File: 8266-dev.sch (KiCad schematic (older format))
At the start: 17 parts, among them J1 USB_B_Micro, U1 ESP8266-12F_ESP-12F, U2 FT231XS

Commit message: updated to v1
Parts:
- removed C3: 0.1uF, symbol Device:C
- removed C4: 10uF, symbol Device:C
- removed C5, C6: C, symbol Device:C
- removed J1: USB_B_Micro, symbol Connector:USB_B_Micro
- removed R5, R6: R, symbol Device:R
- removed U2: FT231XS, Package_SO:SSOP-20_3.9x8.7mm_P0.635mm, symbol Interface_USB:FT231XS
- added J1, J2: Conn_01x05_Female, digikey-kicad-library:PinHeader_1x5_P2.5mm_Drill1.1mm, symbol Connector:Conn_01x05_Female
- added J3: Conn_01x06_Female, Connector_PinHeader_2.54mm:PinHeader_1x06_P2.54mm_Vertical, symbol Connector:Conn_01x06_Female
- added J4: Conn_01x03_Female, digikey-kicad-library:PinHeader_1x3_P2.54_Drill1.1mm, symbol Connector:Conn_01x03_Female
- BT1: footprint (none) -> Battery:BatteryHolder_MPD_BC2003_1x2032
- C2: footprint Capacitor_SMD:C_0603_1608Metric -> Capacitor_SMD:C_1206_3216Metric
- S1: footprint 430152070826:430152070826 -> digikey-kicad-library:Switch_Tactile_SMD_6x6mm
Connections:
- net labels added: ADC, CS0, IO10, IO12, IO13, IO14, IO16, IO2, IO4, IO5, IO9, MISO, MOSI, SCLK, rx, tx
- net labels removed: +3V3, D+, D-, RXD, TXD
- wire segments 41 -> 15
- no-connect marks 16 -> 2
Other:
- note removed: "FT231X IC"
- note removed: "USB INPUT"
- moved on the sheet: R3, S1

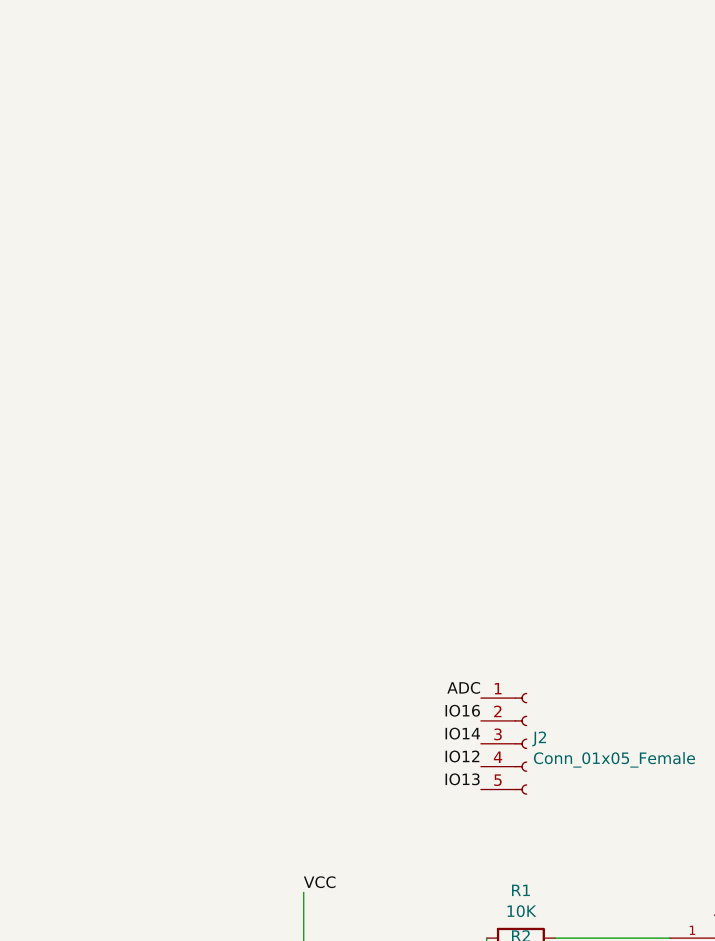
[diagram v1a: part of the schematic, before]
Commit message: added logic level shifter and some WS2812B's
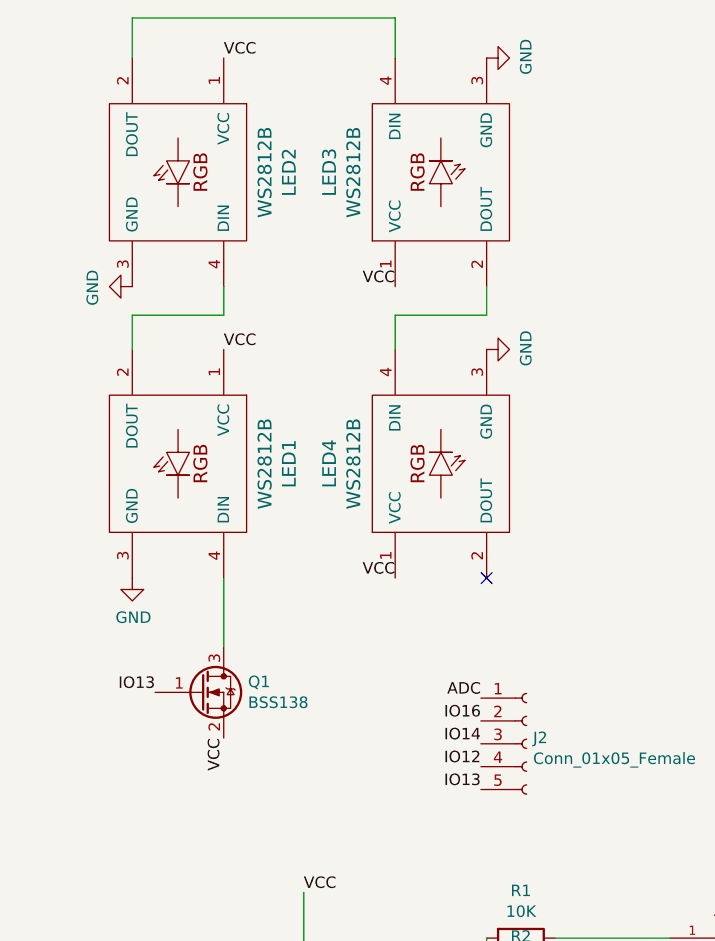
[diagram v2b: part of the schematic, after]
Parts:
- added LED1, LED2, LED3, LED4: WS2812B, LED_SMD:LED_WS2812B_PLCC4_5.0x5.0mm_P3.2mm, symbol ws2812b:WS2812B
- added Q1: BSS138, Package_TO_SOT_SMD:SOT-23, symbol Transistor_FET:BSS138
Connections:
- wire segments 15 -> 25
- no-connect marks 2 -> 3
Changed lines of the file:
@@
 Text Label 4800 6250 1    50   ~ 0
 SCLK
+Text Label 1900 3725 3    50   ~ 0
+VCC
+$Comp
+L Transistor_FET:BSS138 Q1
+U 1 1 5D2FF3C8
+P 1800 3525
+F 0 "Q1" H 2006 3571 50  0000 L CNN
+F 1 "BSS138" H 2006 3480 50  0000 L CNN
+F 2 "Package_TO_SOT_SMD:SOT-23" H 2000 3450 50  0001 L CIN
+F 3 "https://www.fairchildsemi.com/datasheets/BS/BSS138.pdf" H 1800 3525 50  0001 L CNN
+	1    1800 3525
+	1    0    0    -1
+$EndComp
+$Comp
+L ws2812b:WS2812B LED1
+U 1 1 5D31BE71
+P 1700 2525
+F 0 "LED1" H 1700 3012 60  0000 C CNN
+F 1 "WS2812B" H 1700 2906 60  0000 C CNN
+F 2 "LED_SMD:LED_WS2812B_PLCC4_5.0x5.0mm_P3.2mm" V 1650 2525 60  0001 C CNN
+F 3 "" V 1650 2525 60  0000 C CNN
+	1    1700 2525
+	0    1    1    0
+$EndComp
+Wire Wire Line
+	1900 3325 1900 3025
+$Comp
+L power:GND #PWR01
+U 1 1 5D31F7E8
+P 1500 3025
+F 0 "#PWR01" H 1500 2775 50  0001 C CNN
+F 1 "GND" H 1505 2852 50  0000 C CNN
+F 2 "" H 1500 3025 50  0001 C CNN
+F 3 "" H 1500 3025 50  0001 C CNN
+	1    1500 3025
+	1    0    0    -1
+$EndComp
+Text Label 1600 3525 2    50   ~ 0
+IO13
+Text Label 1900 2025 0    50   ~ 0
+VCC
+Text Label 1900 750  0    50   ~ 0
+VCC
+$Comp
+L ws2812b:WS2812B LED2
+U 1 1 5D33F0B1
+P 1700 1250
+F 0 "LED2" H 1700 1737 60  0000 C CNN
+F 1 "WS2812B" H 1700 1631 60  0000 C CNN
+F 2 "LED_SMD:LED_WS2812B_PLCC4_5.0x5.0mm_P3.2mm" V 1650 1250 60  0001 C CNN
+F 3 "" V 1650 1250 60  0000 C CNN
+	1    1700 1250
+	0    1    1    0
+$EndComp
+Wire Wire Line
+	1500 2025 1500 1875
+Wire Wire Line
+	1500 1875 1900 1875
+Wire Wire Line
+	1900 1875 1900 1750
+$Comp
+L power:GND #PWR02
+U 1 1 5D343D9C
+P 1500 1750
+F 0 "#PWR02" H 1500 1500 50  0001 C CNN
+F 1 "GND" H 1505 1577 50  0000 C CNN
+F 2 "" H 1500 1750 50  0001 C CNN
+F 3 "" H 1500 1750 50  0001 C CNN
+	1    1500 1750
+	0    1    1    0
+$EndComp
+$Comp
+L ws2812b:WS2812B LED3
+U 1 1 5D3463F4
+P 2850 1250
+F 0 "LED3" H 2850 1737 60  0000 C CNN
+F 1 "WS2812B" H 2850 1631 60  0000 C CNN
+F 2 "LED_SMD:LED_WS2812B_PLCC4_5.0x5.0mm_P3.2mm" V 2800 1250 60  0001 C CNN
+F 3 "" V 2800 1250 60  0000 C CNN
+	1    2850 1250
+	0    -1   -1   0
+$EndComp
+Text Label 2650 1750 2    50   ~ 0
+VCC
+$Comp
+L power:GND #PWR03
+U 1 1 5D347748
+P 3050 750
+F 0 "#PWR03" H 3050 500 50  0001 C CNN
+F 1 "GND" H 3055 577 50  0000 C CNN
+F 2 "" H 3050 750 50  0001 C CNN
+F 3 "" H 3050 750 50  0001 C CNN
+	1    3050 750
+	0    -1   -1   0
+$EndComp
+Wire Wire Line
+	1500 750  1500 575
+Wire Wire Line
+	1500 575  2650 575
+Wire Wire Line
+	2650 575  2650 750
+$Comp
+L ws2812b:WS2812B LED4
+U 1 1 5D34B87E
+P 2850 2525
+F 0 "LED4" H 2850 3012 60  0000 C CNN
+F 1 "WS2812B" H 2850 2906 60  0000 C CNN
+F 2 "LED_SMD:LED_WS2812B_PLCC4_5.0x5.0mm_P3.2mm" V 2800 2525 60  0001 C CNN
+F 3 "" V 2800 2525 60  0000 C CNN
+	1    2850 2525
+	0    -1   -1   0
+$EndComp
+$Comp
+L power:GND #PWR04
+U 1 1 5D34DD79
+P 3050 2025
+F 0 "#PWR04" H 3050 1775 50  0001 C CNN
+F 1 "GND" H 3055 1852 50  0000 C CNN
+F 2 "" H 3050 2025 50  0001 C CNN
+F 3 "" H 3050 2025 50  0001 C CNN
+	1    3050 2025
+	0    -1   -1   0
+$EndComp
+Text Label 2650 3025 2    50   ~ 0
+VCC
+Wire Wire Line
+	3050 1750 3050 1875
+Wire Wire Line
+	3050 1875 2650 1875
+Wire Wire Line
+	2650 1875 2650 2025
+NoConn ~ 3050 3025
 $EndSCHEMATC

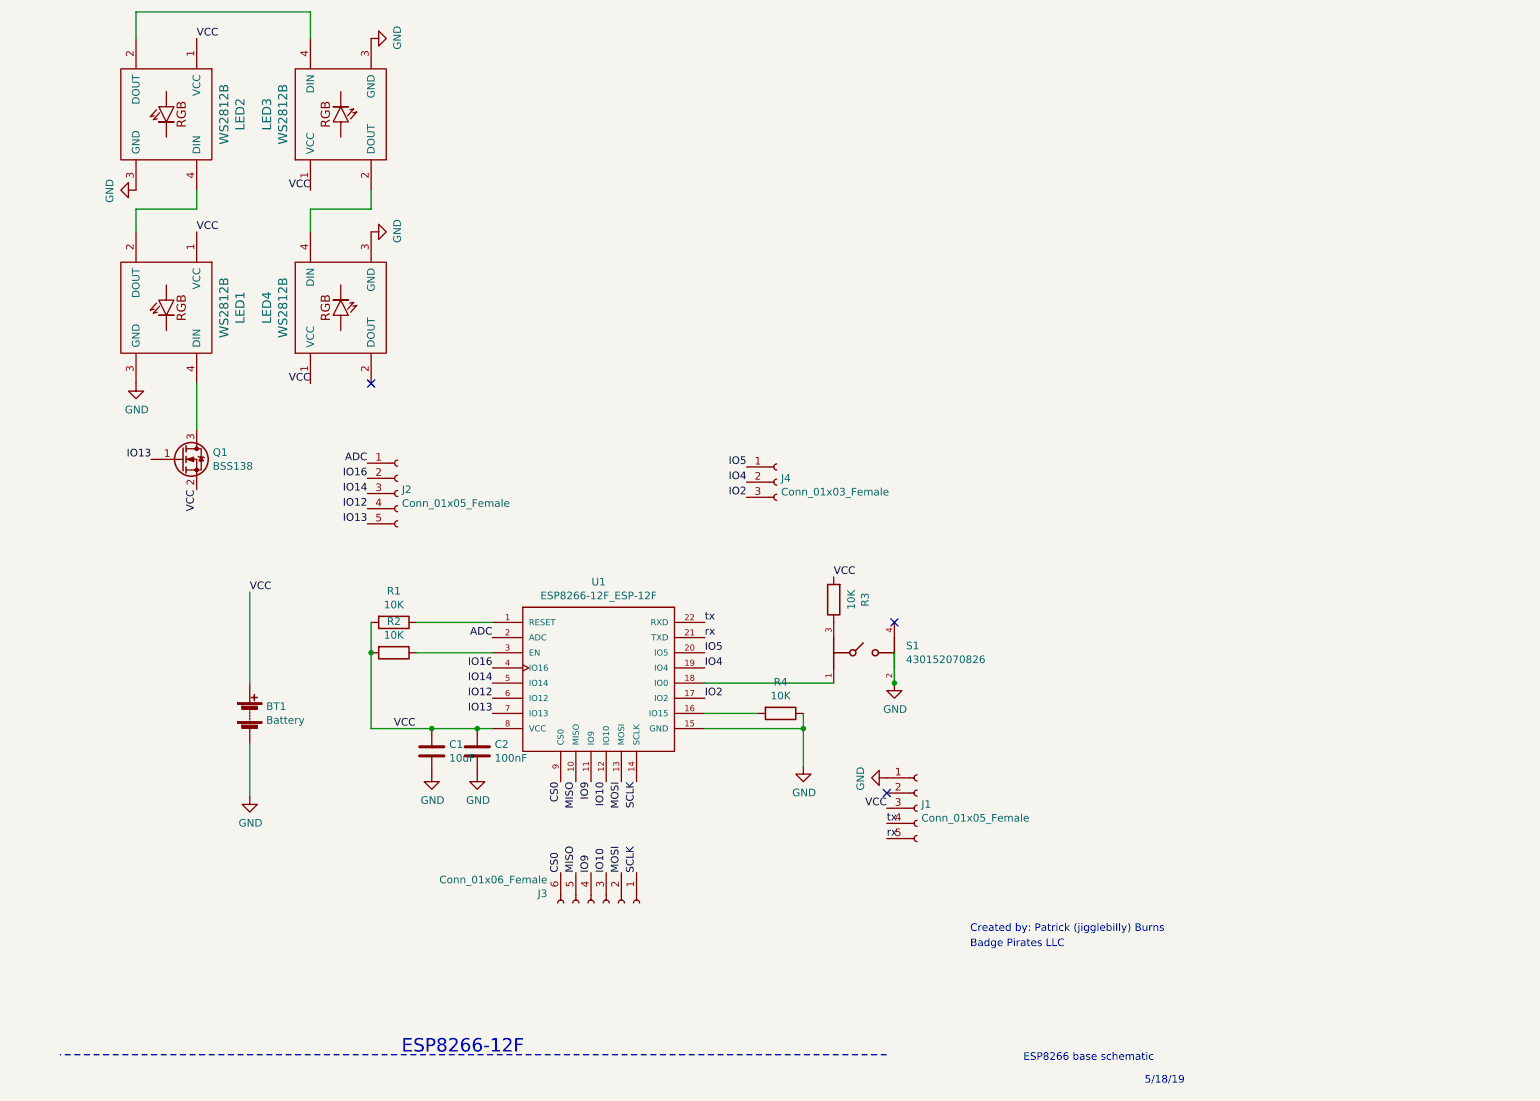
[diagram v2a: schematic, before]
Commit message: added power light, CH330N, and some neopixels
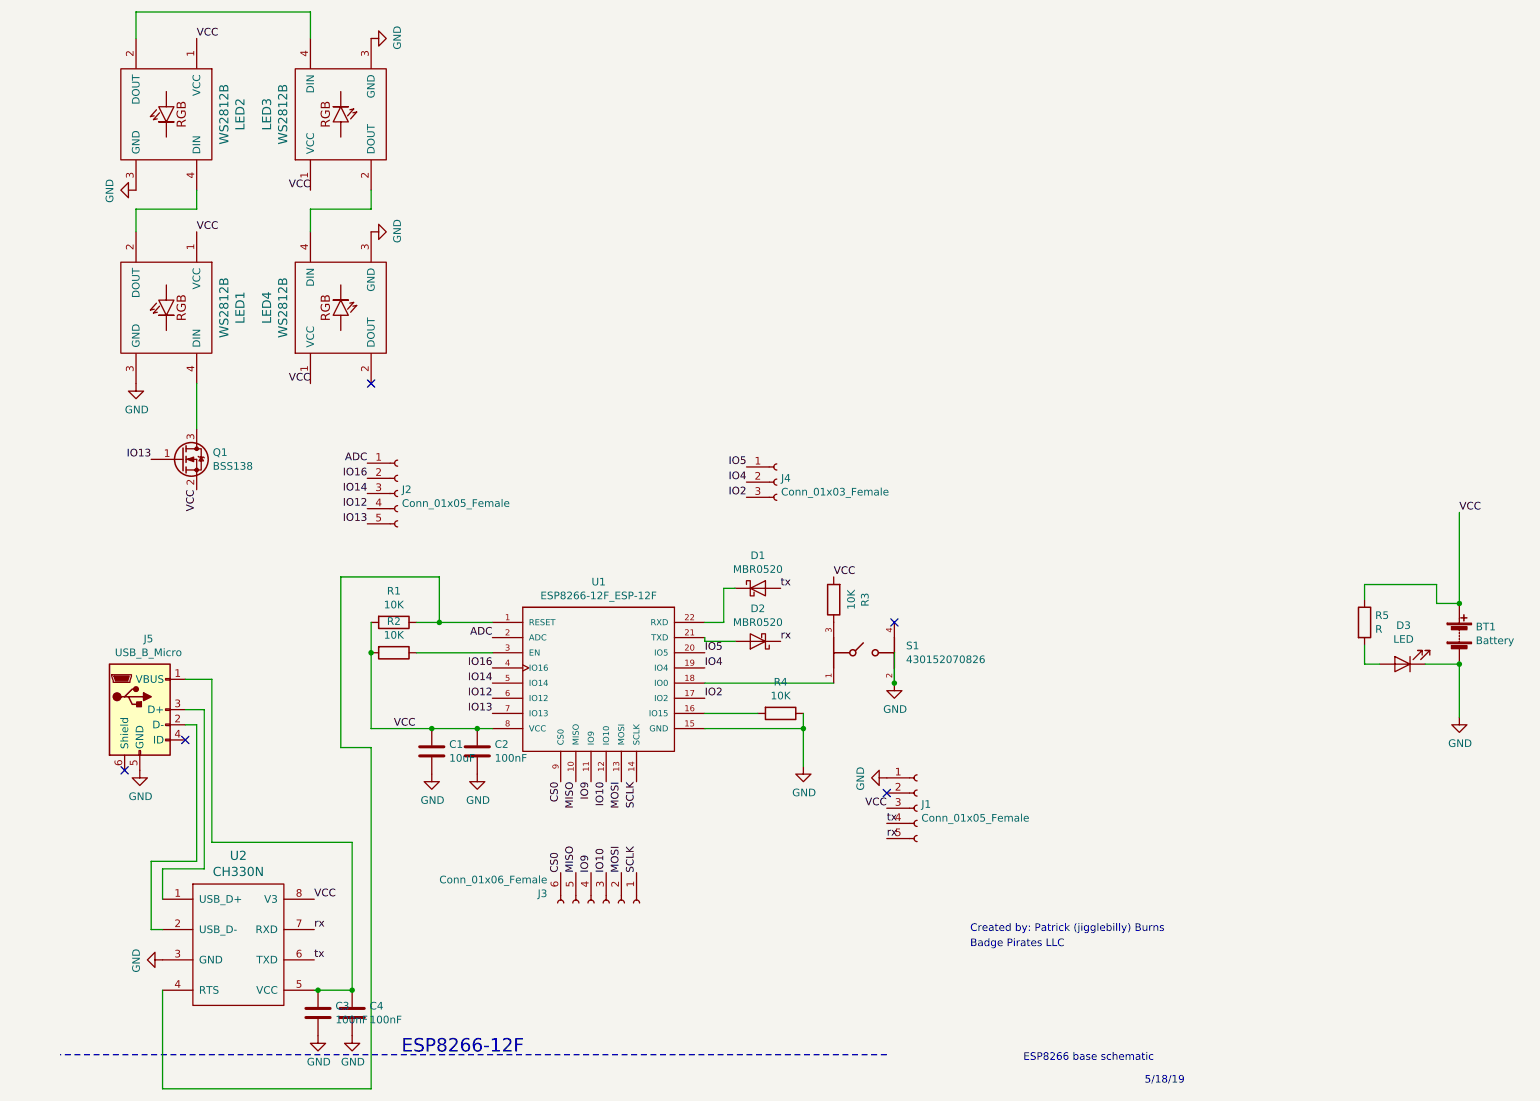
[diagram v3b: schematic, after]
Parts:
- added C3, C4: 100nF, Capacitor_SMD:C_1206_3216Metric, symbol Device:C
- added D1, D2: MBR0520, Diode_SMD:D_SOD-123, symbol Diode:MBR0520
- added D3: LED, LED_SMD:LED_1206_3216Metric_Pad1.42x1.75mm_HandSolder, symbol Device:LED
- added J5: USB_B_Micro, Connector_USB:USB_Micro-B_Molex-105017-0001, symbol Connector:USB_B_Micro
- added R5: R, Resistor_SMD:R_1206_3216Metric, symbol Device:R
- added U2: CH330N, Package_SO:SOIC-8_3.9x4.9mm_P1.27mm, symbol CH330N:CH330N
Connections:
- wire segments 25 -> 60
- no-connect marks 3 -> 5
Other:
- moved on the sheet: BT1

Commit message: update
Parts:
- removed D1, D2: MBR0520, Diode_SMD:D_SOD-123, symbol Diode:MBR0520
- added C5: 100nF, Capacitor_SMD:C_1206_3216Metric, symbol Device:C
- D3: value LED -> GREEN LED
- J1: value Conn_01x05_Female -> Programming headers
- J2: value Conn_01x05_Female -> Left breakout
- J3: value Conn_01x06_Female -> Bottom breakout
- J4: value Conn_01x03_Female -> Right breakout
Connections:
- net GND: now also J5.6 (Shield), C5.1
- net VCC: now also C5.2
- net rx: now also U1.22 (RXD)
- net tx: now also U1.21 (TXD)
- net RTS: now reaches R1.1, U1.1 (RESET), U2.4 (RTS)
- net VBUS: now reaches C3.1, C4.1, J5.1 (VBUS), U2.5 (VCC)
- net D-: now reaches J5.2 (D-), U2.2 (USB_D-)
- net D+: now reaches J5.3 (D+), U2.1 (USB_D+)
- no-connect marks 5 -> 4
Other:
- note added: "jiggleforce.com"
- note removed: "Badge Pirates LLC"
- note removed: "ESP8266-12F"
- moved on the sheet: C4, J1, J2, J3, J4, J5, R1
